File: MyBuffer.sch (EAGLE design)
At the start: 72 parts, among them Q1 BD140, Q2 BD139, Q3 BD140, Q4 BD139, T10 BD140, T11 BD139, T12 BD140, T9 BD139

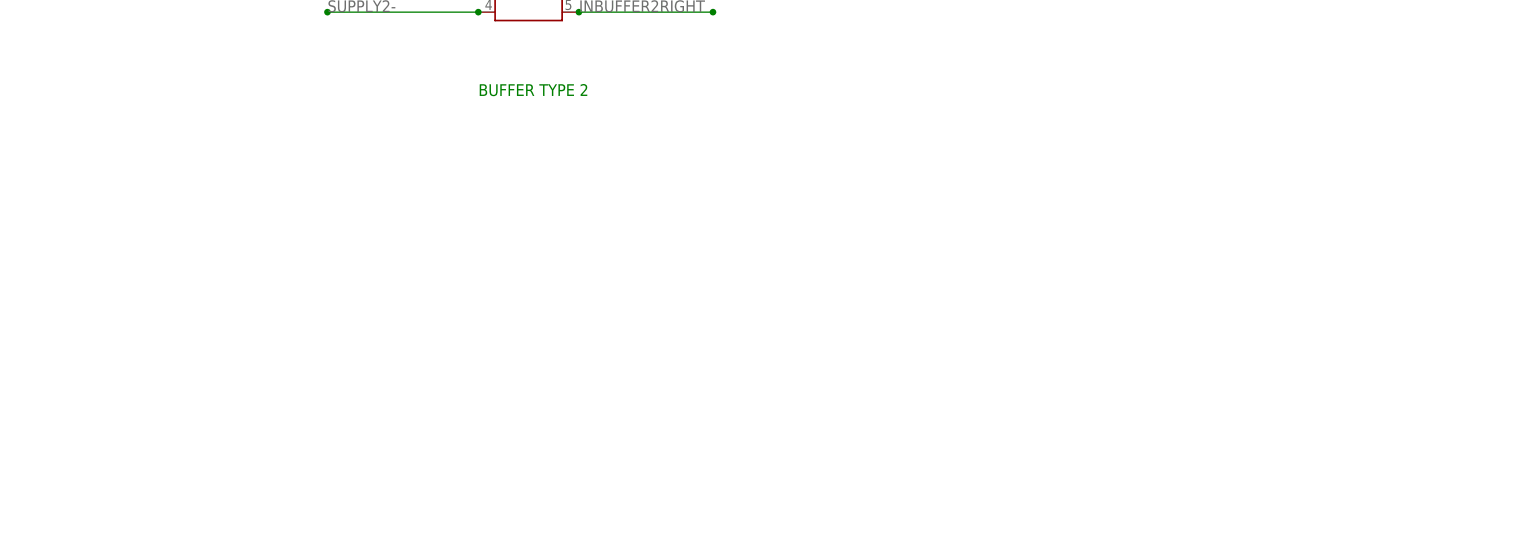
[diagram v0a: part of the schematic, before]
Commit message: add module capacitance multiplier and buffer ground
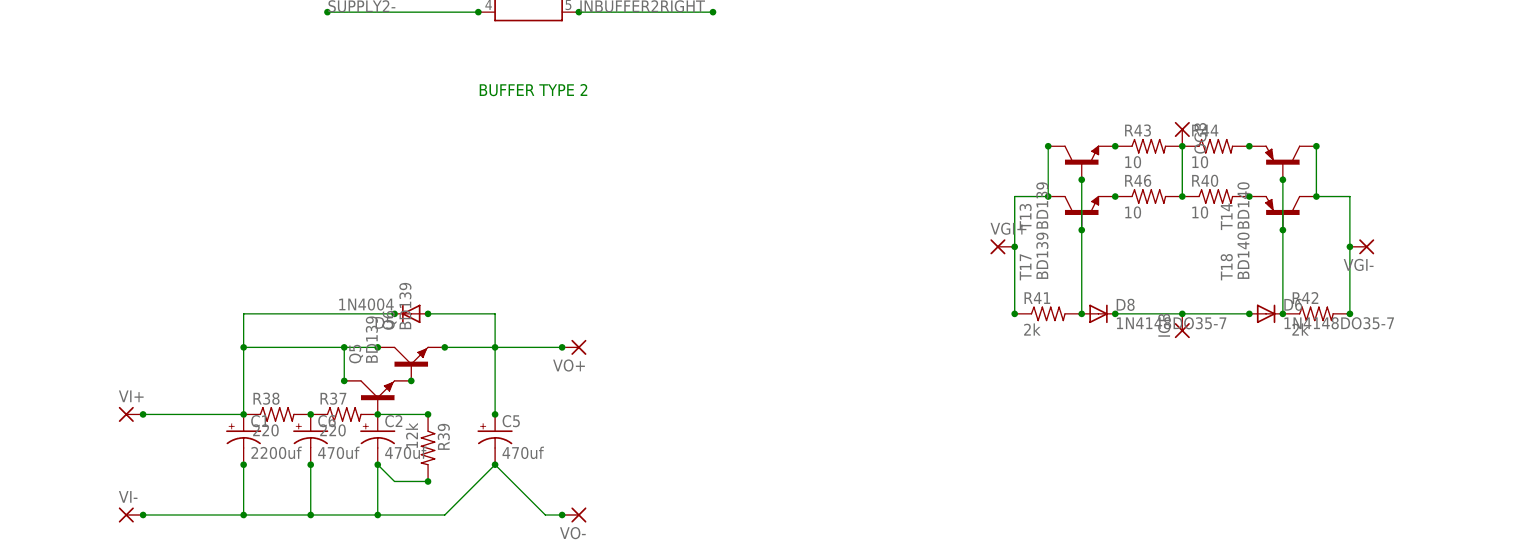
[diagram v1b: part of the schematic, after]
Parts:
- added C1: 2200uf, rcl:CPOL-USE7.5-16
- added C2, C5, C6: 470uf, rcl:CPOL-USE7.5-16
- added D5: 1N4004, diode:1N4004
- added D6, D8: 1N4148DO35-7, diode:1N4148DO35-7
- added IGB, OGB, VGI+, VGI-, VI+, VI-, VO+, VO-: (no value), wirepad:2,54/0,8
- added Q5, Q6: BD139, transistor-power:BD139
- added R37, R38: 220, resistor:R-US_0207/10
- added R39: 12k, resistor:R-US_0207/10
- added R40, R43, R44, R46: 10, resistor:R-US_0207/10
- added R41, R42: 2k, resistor:R-US_0207/10
- added T13, T17: BD139, transistor-npn:BD139
- added T14, T18: BD140, transistor-pnp:BD140
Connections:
- new net N$32: C2.+, Q5.B, R37.2, R39.1
- new net N$33: Q5.E, Q6.B
- new net N$35: C6.+, R37.1, R38.2
- new net N$36: C1.+, D5.C, Q5.C, Q6.C, R38.1, VI+.P
- new net N$37: C1.-, C2.-, C5.-, C6.-, R39.2, VI-.P, VO-.P
- new net N$39: C5.+, D5.A, Q6.E, VO+.P
- new net N$40: OGB.P, R40.1, R43.2, R44.1, R46.2
- new net N$42: R46.1, T17.E
- new net N$44: R40.2, T18.E
- new net N$45: D6.C, R42.1, T14.B, T18.B
- new net N$46: D8.A, R41.2, T13.B, T17.B
- new net N$48: R41.1, T13.C, T17.C, VGI+.P
- new net N$50: R42.2, T14.C, T18.C, VGI-.P
- new net N$51: D6.A, D8.C, IGB.P
- new net N$52: R43.1, T13.E
- new net N$54: R44.2, T14.E

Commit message: Initial Commit
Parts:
- T13, T17: device transistor-npn:BD139 -> transistor-power:BD139
- T14, T18: device transistor-pnp:BD140 -> transistor-power:BD140
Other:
- note added: "BUFFER GROUND"
- note added: "Simple Capacitance Multiplier"
- moved on the sheet: C1, C2, C5, C6, D5, D6, D8, IGB, OGB, Q5, Q6, R37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
